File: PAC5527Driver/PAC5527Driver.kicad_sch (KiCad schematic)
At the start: 80 parts, among them J1 Conn_01x08, J2 Conn_01x04, J3 Conn_01x04, J4 Conn_01x02, U1 USBLC6-2SC6, U2 SN65HVD230, U3 MA730, U4 PAC5527, U5 HT7550-1-SOT89

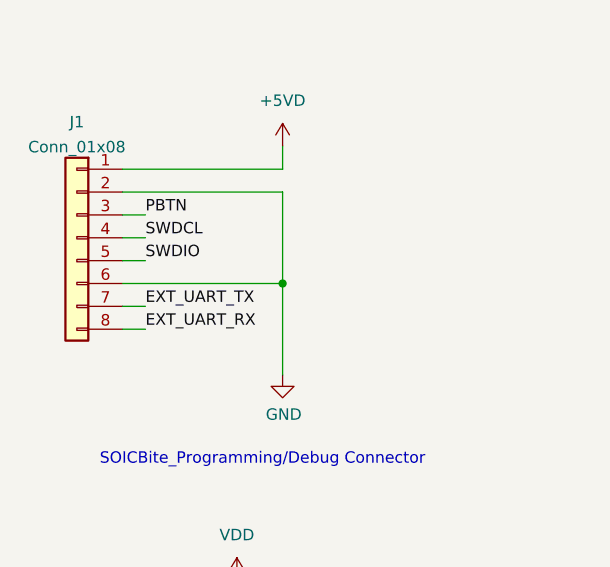
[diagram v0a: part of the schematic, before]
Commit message: MCU fanout, power stage roughed in, setup is now 6L
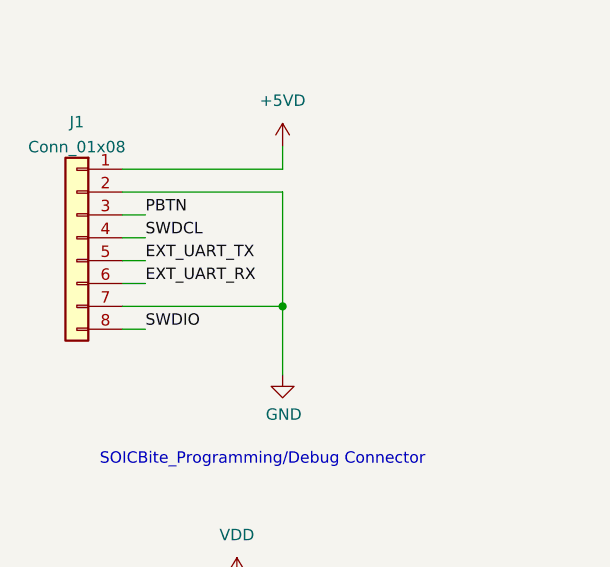
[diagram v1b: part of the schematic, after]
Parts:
- L1: footprint Inductor_SMD:L_Bourns-SRN4018 -> Inductor_SMD:L_Changjiang_FNR3010S
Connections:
- net EXT_UART_RX: now also J1.6 (Pin_6); no longer J1.8 (Pin_8)
- net EXT_UART_TX: now also J1.5 (Pin_5); no longer J1.7 (Pin_7)
- net GND: now also J1.7 (Pin_7); no longer J1.6 (Pin_6)
- net SWDIO: now also J1.8 (Pin_8); no longer J1.5 (Pin_5)
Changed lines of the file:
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@@
   (junction (at 129.54 162.56) (diameter 0) (color 0 0 0 0)
   )
-  (junction (at 55.88 55.88) (diameter 0) (color 0 0 0 0)
-  )
   (junction (at 163.83 247.65) (diameter 0) (color 0 0 0 0)
   )
@@
   )
   (junction (at 193.04 38.1) (diameter 0) (color 0 0 0 0)
+  )
+  (junction (at 55.88 58.42) (diameter 0) (color 0 0 0 0)
   )
   (junction (at 368.3 132.08) (diameter 0) (color 0 0 0 0)
@@
     (stroke (width 0) (type default))
   )
+  (wire (pts (xy 38.1 55.88) (xy 40.64 55.88))
+    (stroke (width 0) (type default))
+  )
   (wire (pts (xy 133.35 262.89) (xy 133.35 257.81))
     (stroke (width 0) (type default))
@@
     (stroke (width 0) (type default))
   )
+  (wire (pts (xy 38.1 58.42) (xy 55.88 58.42))
+    (stroke (width 0) (type default))
+  )
   (wire (pts (xy 227.33 147.32) (xy 242.57 147.32))
     (stroke (width 0) (type default))
@@
     (stroke (width 0) (type default))
   )
+  (wire (pts (xy 55.88 58.42) (xy 55.88 66.04))
+    (stroke (width 0) (type default))
+  )
   (wire (pts (xy 248.92 262.89) (xy 260.35 262.89))
     (stroke (width 0) (type default))
@@
     (stroke (width 0) (type default))
   )
-  (wire (pts (xy 55.88 55.88) (xy 55.88 66.04))
+  (wire (pts (xy 55.88 45.72) (xy 55.88 58.42))
     (stroke (width 0) (type default))
   )
@@
     (stroke (width 0) (type default))
   )
-  (wire (pts (xy 38.1 58.42) (xy 40.64 58.42))
-    (stroke (width 0) (type default))
-  )
   (wire (pts (xy 368.3 60.96) (xy 368.3 66.04))
     (stroke (width 0) (type default))
@@
     (stroke (width 0) (type default))
   )
-  (wire (pts (xy 55.88 45.72) (xy 55.88 55.88))
-    (stroke (width 0) (type default))
-  )
   (wire (pts (xy 342.9 132.08) (xy 342.9 134.62))
     (stroke (width 0) (type default))
@@
   )
   (wire (pts (xy 205.74 144.78) (xy 205.74 147.32))
-    (stroke (width 0) (type default))
-  )
-  (wire (pts (xy 38.1 55.88) (xy 55.88 55.88))
     (stroke (width 0) (type default))
   )
@@
     (effects (font (size 1.27 1.27)) (justify left bottom))
   )
-  (label "EXT_UART_RX" (at 40.64 60.96 0) (fields_autoplaced)
-    (effects (font (size 1.27 1.27)) (justify left bottom))
-  )
   (label "ENC_MISO" (at 292.1 78.74 0) (fields_autoplaced)
     (effects (font (size 1.27 1.27)) (justify left bottom))
   )
   (label "LED_IN" (at 292.1 66.04 0) (fields_autoplaced)
+    (effects (font (size 1.27 1.27)) (justify left bottom))
+  )
+  (label "EXT_UART_RX" (at 40.64 55.88 0) (fields_autoplaced)
     (effects (font (size 1.27 1.27)) (justify left bottom))
   )
@@
     (effects (font (size 1.27 1.27)) (justify left bottom))
   )
-  (label "EXT_UART_TX" (at 40.64 58.42 0) (fields_autoplaced)
-    (effects (font (size 1.27 1.27)) (justify left bottom))
-  )
   (label "US" (at 347.98 50.8 0) (fields_autoplaced)
     (effects (font (size 1.27 1.27)) (justify left bottom))
   )
+  (label "SWDIO" (at 40.64 60.96 0) (fields_autoplaced)
+    (effects (font (size 1.27 1.27)) (justify left bottom))
+  )
   (label "CAN_L" (at 172.72 149.86 0) (fields_autoplaced)
     (effects (font (size 1.27 1.27)) (justify left bottom))
@@
     (effects (font (size 1.27 1.27)) (justify left bottom))
   )
+  (label "EXT_UART_TX" (at 40.64 53.34 0) (fields_autoplaced)
+    (effects (font (size 1.27 1.27)) (justify left bottom))
+  )
   (label "UART_RX" (at 292.1 43.18 0) (fields_autoplaced)
     (effects (font (size 1.27 1.27)) (justify left bottom))
@@
   )
   (label "VH" (at 294.64 124.46 0) (fields_autoplaced)
-    (effects (font (size 1.27 1.27)) (justify left bottom))
-  )
-  (label "SWDIO" (at 40.64 53.34 0) (fields_autoplaced)
     (effects (font (size 1.27 1.27)) (justify left bottom))
   )
@@
       (effects (font (size 1.27 1.27)))
     )
-    (property "Footprint" "Inductor_SMD:L_Bourns-SRN4018" (at 113.03 38.1 0)
+    (property "Footprint" "Inductor_SMD:L_Changjiang_FNR3010S" (at 113.03 38.1 0)
       (effects (font (size 1.27 1.27)) hide)
     )

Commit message: output via stitching
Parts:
- D3: footprint Diode_SMD:D_SMA -> Diode_SMD:D_SOD-123
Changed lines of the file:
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@@
       (effects (font (size 1.27 1.27)) (justify left))
     )
-    (property "Footprint" "Diode_SMD:D_SMA" (at 60.96 209.55 0)
+    (property "Footprint" "Diode_SMD:D_SOD-123" (at 60.96 209.55 0)
       (effects (font (size 1.27 1.27)) hide)
     )

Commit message: initial layout pass
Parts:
- removed C15, C17, C28: 10uF, Capacitor_SMD:C_1210_3225Metric, symbol Device:C
- removed R20, R21, R22: 0.1, Resistor_SMD:R_1206_3216Metric, symbol Device:R
- added R20, R21, R22: 0.1, PAC5527Driver:RShunt_1206_3216Metric, symbol Device:R_Shunt
- C7: footprint Capacitor_SMD:C_0603_1608Metric -> Capacitor_SMD:C_0402_1005Metric
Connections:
- net GND: now also R20.4, R21.4, R22.4; no longer RN1.1 (R1.1), RN1.3 (R3.1), RN1.5 (R5.1)
- net at Q1.SL: now also R20.1; no longer RN1.2 (R2.1)
- net at Q2.SL: now also R21.1; no longer RN1.4 (R4.1)
- net at Q3.SL: now also R22.1; no longer RN1.6 (R6.1)
- new net: R20.2, RN1.2 (R2.1)
- new net: R21.2, RN1.4 (R4.1)
- new net: R22.3, RN1.5 (R5.1)
- new net: R22.2, RN1.6 (R6.1)
- new net: R20.3, RN1.1 (R1.1)
- new net: R21.3, RN1.3 (R3.1)
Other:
- moved on the sheet: C19, C22, C23, C24, C27, C29, C30, C31, C32, C33, C34, C39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

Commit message: redone layout
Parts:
- removed C22, C39, C40: 10uF, Capacitor_SMD:C_1210_3225Metric, symbol Device:C
- removed D6: NUP2105L, Package_TO_SOT_SMD:SOT-23, symbol Power_Protection:NUP2105L
- removed J2, J3: Conn_01x04, Connector_JST:JST_GH_SM04B-GHS-TB_1x04-1MP_P1.25mm_Horizontal, symbol Connector_Generic:Conn_01x04
- removed R10, R8: 10k, Resistor_SMD:R_0402_1005Metric, symbol Device:R
- removed R7: 100, Resistor_SMD:R_0402_1005Metric, symbol Device:R
- removed U2: SN65HVD230, Package_SO:SOIC-8_3.9x4.9mm_P1.27mm, symbol Interface_CAN_LIN:SN65HVD230
- removed U5: HT7550-1-SOT89, Package_TO_SOT_SMD:SOT-89-3, symbol Regulator_Linear:HT75xx-1-SOT89
- added C15, C17, C21, C26, C28, C35, C36, C37, C38: 10uF, Capacitor_SMD:C_1210_3225Metric, symbol Device:C
- added D5: NUP2105L, Package_TO_SOT_SMD:SOT-23, symbol Power_Protection:NUP2105L
- added J2, J3: Conn_01x04_MountingPin, Connector_JST:JST_GH_SM04B-GHS-TB_1x04-1MP_P1.25mm_Horizontal, symbol Connector_Generic_MountingPin:Conn_01x04_MountingPin
- added J5: Conn_01x06_MountingPin, Connector_JST:JST_GH_BM06B-GHS-TBT_1x06-1MP_P1.25mm_Vertical, symbol Connector_Generic_MountingPin:Conn_01x06_MountingPin
- added J6: Conn_01x03, Connector_PinHeader_2.54mm:PinHeader_1x03_P2.54mm_Vertical, symbol Connector_Generic:Conn_01x03
- added J8: Conn_01x03_MountingPin, Connector_JST:JST_GH_BM03B-GHS-TBT_1x03-1MP_P1.25mm_Vertical, symbol Connector_Generic_MountingPin:Conn_01x03_MountingPin
- added R2: 10k, Resistor_SMD:R_0402_1005Metric, symbol Device:R
- added R4: 100, Resistor_SMD:R_0402_1005Metric, symbol Device:R
- added U2: TCAN330G, Package_TO_SOT_SMD:SOT-23-8, symbol Interface_CAN_LIN:TCAN330G
- added U6: HT7533-1-SOT89, Package_TO_SOT_SMD:SOT-89-3, symbol Regulator_Linear:HT75xx-1-SOT89
- H1, H2: footprint PAC5527Driver:MountingHole_SLOT_1.6_M1.5_DIN965_Pad_TopBottom -> MountingHole:MountingHole_2.2mm_M2_DIN965_Pad_TopBottom
- H3, H4, H5: footprint PAC5527Driver:MountingHole_SLOT_2.2mm_M2_DIN965_Pad_TopBottom -> MountingHole:MountingHole_2.2mm_M2_DIN965_Pad_TopOnly
- R9: value 100 -> 10k
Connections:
- net +12V: now also U6.2 (VIN)
- net CAN_H: now also D5.1 (K), J2.2 (Pin_2), J3.2 (Pin_2), R2.1, U2.7 (CANH)
- net CAN_L: now also D5.2 (K), J2.3 (Pin_3), J3.3 (Pin_3), R2.2, U2.6 (CANL)
- net CAN_SLP: now also R4.1
- net ENC_MISO: now also J5.5 (Pin_5)
- net ENC_MOSI: now also J5.4 (Pin_4)
- net ENC_SCLK: now also J5.2 (Pin_2)
- net EXT_UART_RX: now also J6.2 (Pin_2)
- net EXT_UART_TX: now also J6.3 (Pin_3)
- net GND: now also C4.2, C15.2, C17.2, C21.2, C26.2, C28.2, C35.2, C36.2, C37.2, C38.2, D5.3 (A), J2.1 (Pin_1), J2.MP (MountPin), J3.1 (Pin_1), J3.MP (MountPin), J5.6 (Pin_6), J5.MP (MountPin), J6.1 (Pin_1), J8.3 (Pin_3), J8.MP (MountPin), U2.2 (GND), U6.1 (GND); no longer C4.1
- net MB_ID_0: now also J8.2 (Pin_2)
- net MB_ID_1: now also J8.1 (Pin_1)
- net VDC: now also C15.1, C17.1, C21.1, C26.1, C28.1, C35.1, C36.1, C37.1, C38.1
- net VDD: now also J5.1 (Pin_1), U2.3 (VCC), U6.3 (VOUT)
- net ENC_CS1: now reaches U4.35 (PD5)
- net ENC_CS1: now also J5.3 (Pin_3)
- net at R5.1: now also U2.1 (TXD)
- net at R6.2: now also U2.4 (RXD)
- new net: C4.1, R4.2, U2.8 (S)
- no-connect marks 17 -> 18
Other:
- moved on the sheet: C14, C19, C20, C25, C5, C8, D1, D2, D3, D4, H1, H2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

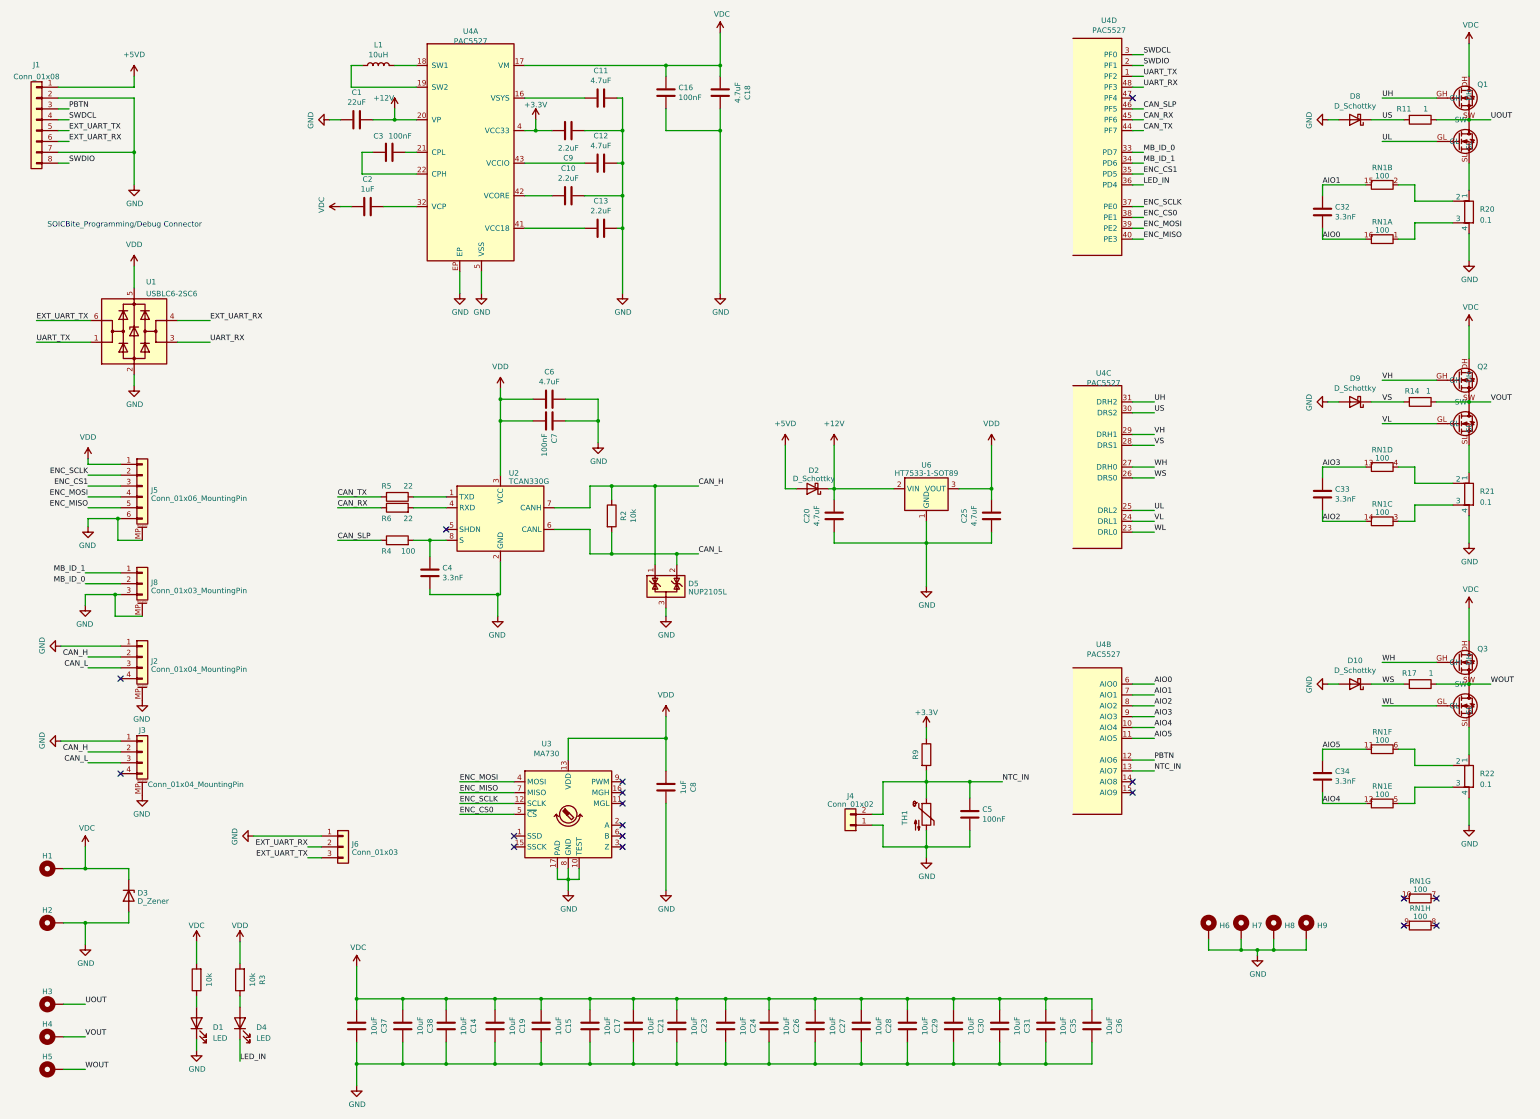
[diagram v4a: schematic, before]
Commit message: spaced out mounting points by 0.5mm
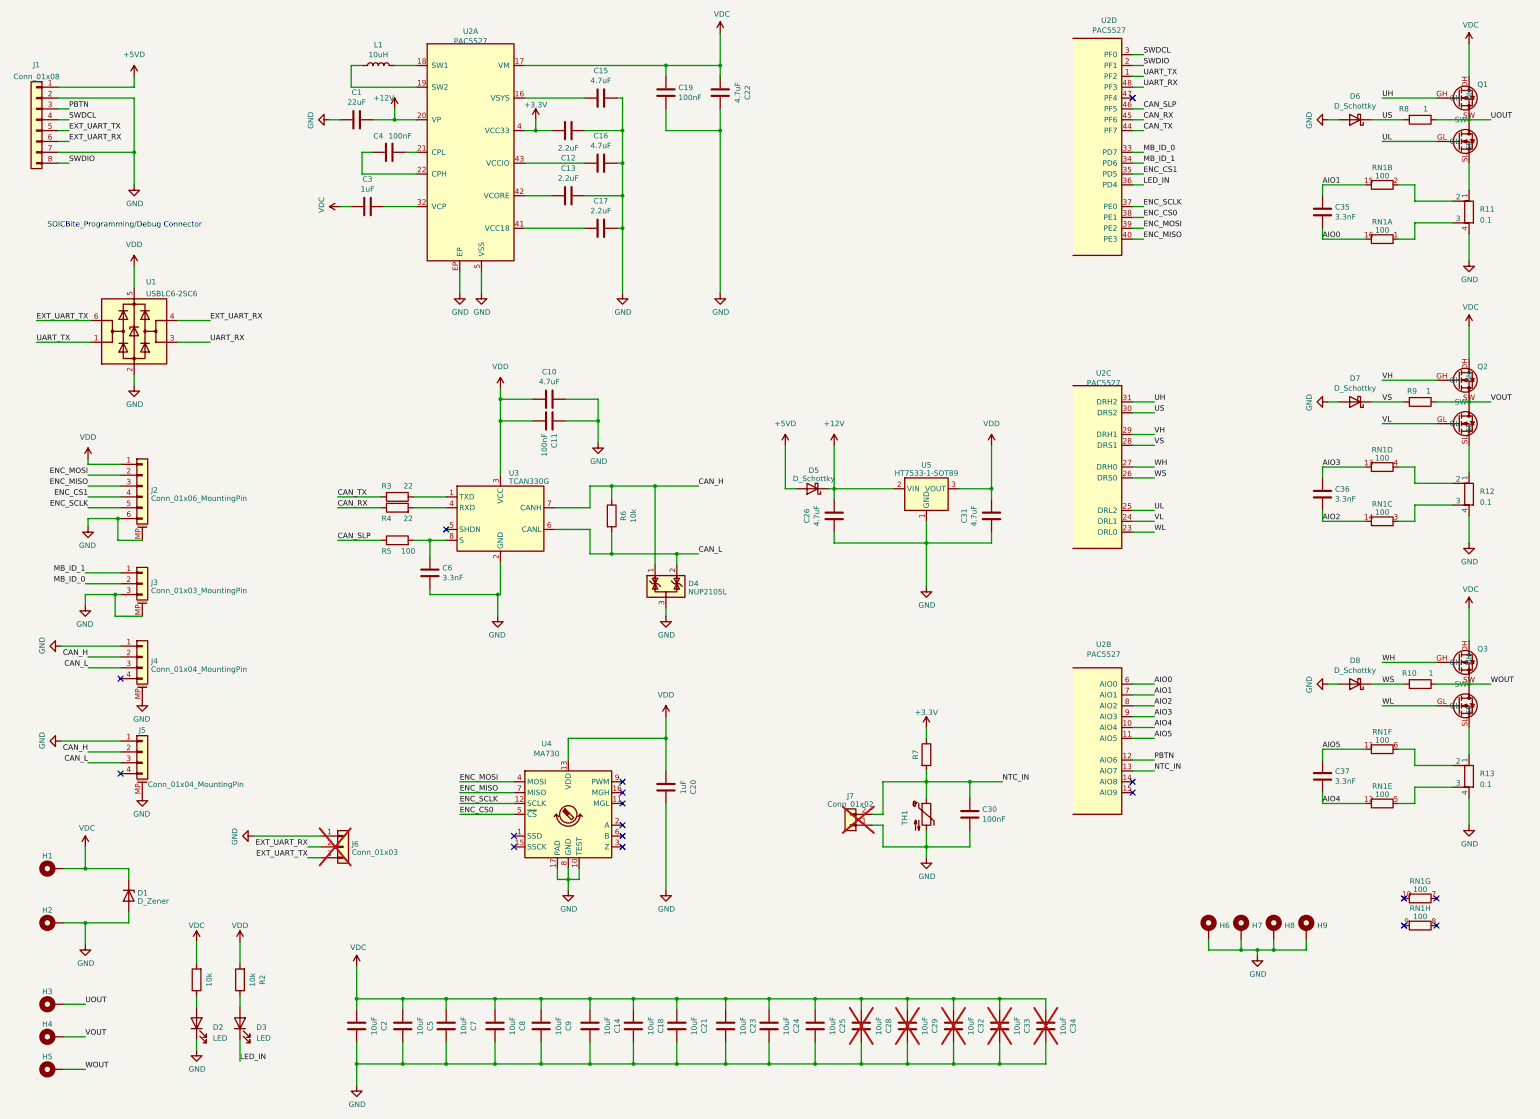
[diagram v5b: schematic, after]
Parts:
- removed C28: 10uF, Capacitor_SMD:C_1210_3225Metric, symbol Device:C
- C28: renamed from C29; now not fitted
- C29: renamed from C30; now not fitted
- C32: renamed from C31; now not fitted
- C33: renamed from C35; now not fitted
- C34: renamed from C36; now not fitted
- H6, H7, H8, H9: footprint MountingHole:MountingHole_2.2mm_M2_ISO7380_Pad_TopBottom -> MountingHole:MountingHole_2.7mm_M2.5_DIN965_Pad_TopBottom
- J6: now not fitted
- J7: renamed from J4; now not fitted
- renumbered C6 to C10, C7 to C11, C9 to C12, C10 to C13, C17 to C14, C11 to C15, C12 to C16, C13 to C17, C21 to C18, C16 to C19, C37 to C2, C8 to C20, C23 to C21, C18 to C22, C24 to C23, C26 to C24, C27 to C25, C20 to C26, C2 to C3, C5 to C30, C25 to C31, C32 to C35, C33 to C36, C34 to C37, C3 to C4, C38 to C5, C4 to C6, C14 to C7, C19 to C8, C15 to C9, D3 to D1, D1 to D2, D4 to D3, D5 to D4, D2 to D5, D8 to D6, D9 to D7, D10 to D8, J5 to J2, J8 to J3, J2 to J4, J3 to J5, R17 to R10, R20 to R11, R21 to R12, R22 to R13, R3 to R2, R5 to R3, R6 to R4, R4 to R5, R2 to R6, R9 to R7, R11 to R8, R14 to R9, U4 to U2, U2 to U3, U3 to U4, U6 to U5
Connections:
- net ENC_CS1: now also J2.4 (Pin_4); no longer J2.3 (Pin_3)
- net ENC_MISO: now also J2.3 (Pin_3); no longer J2.5 (Pin_5)
- net ENC_MOSI: now also J2.2 (Pin_2); no longer J2.4 (Pin_4)
- net ENC_SCLK: now also J2.5 (Pin_5); no longer J2.2 (Pin_2)

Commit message: initial layout
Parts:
- removed C21, C23, C24, C28, C29, C32, C33, C34: 10uF, Capacitor_SMD:C_1210_3225Metric, symbol Device:C
- removed C6: 3.3nF, Capacitor_SMD:C_0402_1005Metric, symbol Device:C
- removed J2: Conn_01x06_MountingPin, Connector_JST:JST_GH_BM06B-GHS-TBT_1x06-1MP_P1.25mm_Vertical, symbol Connector_Generic_MountingPin:Conn_01x06_MountingPin
- removed Q1, Q2, Q3: ~, PAC5527Driver:PG-TDSON-8, symbol PAC5527_MD:IAUC60N04S6L045H
- removed R11, R12, R13: 0.1, PAC5527Driver:RShunt_1206_3216Metric, symbol Device:R_Shunt
- removed U3: TCAN330G, Package_TO_SOT_SMD:SOT-23-8, symbol Interface_CAN_LIN:TCAN330G
- added C12, C14, C15, C17: 10uF, Capacitor_SMD:C_1210_3225Metric, symbol Device:C
- added C3: 100nF, Capacitor_SMD:C_0402_1005Metric, symbol Device:C
- added J2: Conn_01x04_MountingPin, Connector_JST:JST_GH_BM04B-GHS-TBT_1x04-1MP_P1.25mm_Vertical, symbol Connector_Generic_MountingPin:Conn_01x04_MountingPin
- added J3: Conn_01x08_MountingPin, Connector_JST:JST_GH_BM08B-GHS-TBT_1x08-1MP_P1.25mm_Vertical, symbol Connector_Generic_MountingPin:Conn_01x08_MountingPin
- added NT1, NT2, NT3, NT4, NT5, NT6: NetTie_2, NetTie:NetTie-2_SMD_Pad0.5mm, symbol Device:NetTie_2
- added Q1, Q2, Q3, Q4, Q5, Q6: Si7336ADP, Package_SO:PowerPAK_SO-8_Single, symbol Transistor_FET:Si7336ADP
- added R13, R14, R15: R, Resistor_SMD:R_2512_6332Metric, symbol Device:R
- added R5: 100, Resistor_SMD:R_0402_1005Metric, symbol Device:R
- added R7: 10k, Resistor_SMD:R_0402_1005Metric, symbol Device:R
- added U2: SN65HVD233, Package_SO:SOIC-8_3.9x4.9mm_P1.27mm, symbol Interface_CAN_LIN:SN65HVD233
- H6, H7, H8, H9: footprint MountingHole:MountingHole_2.7mm_M2.5_DIN965_Pad_TopBottom -> MountingHole:MountingHole_2.7mm_M2.5_Pad_TopBottom
- R6: renamed from R5; value 100 -> 10k
- renumbered C2 to C1, C1 to C10, C3 to C11, C4 to C13, C20 to C16, C26 to C19, C5 to C2, C12 to C20, C13 to C21, C15 to C22, C16 to C23, C17 to C24, C19 to C26, C22 to C27, C31 to C28, C30 to C29, C37 to C30, C36 to C31, C35 to C32, C7 to C4, C8 to C5, C9 to C6, C10 to C7, C11 to C8, C14 to C9, D8 to D6, D6 to D8, J3 to J4, J4 to J5, J5 to J6, J6 to J7, J7 to J8, R9 to R11, R8 to R12, R6 to R8, R7 to R9, U4 to U3, U2 to U4
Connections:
- net CAN_H: now also U2.7 (CANH)
- net CAN_L: now also U2.6 (CANL)
- net ENC_CS1: now also J3.7 (Pin_7)
- net ENC_MISO: now also J3.6 (Pin_6)
- net ENC_MOSI: now also J3.5 (Pin_5)
- net ENC_SCLK: now also J3.8 (Pin_8)
- net EXT_UART_RX: now also J3.4 (Pin_4)
- net EXT_UART_TX: now also J3.3 (Pin_3)
- net GND: now also R6.1, C12.2, C14.2, C15.2, C17.2, C3.1, J2.4 (Pin_4), J2.MP (MountPin), J3.1 (Pin_1), J3.MP (MountPin), NT2.2, NT4.2, NT6.2, R13.2, R14.2, R15.2, R7.1, U2.2 (GND)
- net SWDCL: now also J2.2 (Pin_2)
- net SWDIO: now also J2.3 (Pin_3)
- net UH: now also Q5.4 (G)
- net UL: now also Q6.4 (G)
- net UOUT: now also Q5.1 (S), Q5.2 (S), Q5.3 (S), Q6.5 (D)
- net VDC: now also C12.1, C14.1, C15.1, C17.1, Q1.5 (D), Q3.5 (D), Q5.5 (D)
- net VDD: now also J2.1 (Pin_1), J3.2 (Pin_2), U2.3 (VCC)
- net VH: now also Q3.4 (G)
- net VL: now also Q4.4 (G)
- net VOUT: now also Q3.1 (S), Q3.2 (S), Q3.3 (S), Q4.5 (D)
- net WH: now also Q1.4 (G)
- net WL: now also Q2.4 (G)
- net WOUT: now also Q1.1 (S), Q1.2 (S), Q1.3 (S), Q2.5 (D)
- net at R6.2: now also C3.2, R5.2, U2.8 (Rs)
- net at RN1.2 (R2.1): now also NT5.1
- net at RN1.4 (R4.1): now also NT3.1
- net at RN1.5 (R5.1): now also NT2.1
- net at RN1.6 (R6.1): now also NT1.1
- net at RN1.1 (R1.1): now also NT6.1
- net at R4.2: now also U2.4 (R)
- net at RN1.3 (R3.1): now also NT4.1
- net at R3.1: now also U2.1 (D)
- net CAN_SLP renamed CAN_STDBY
- net CAN_STDBY: now also R5.1; no longer R6.1
- new net: NT3.2, Q4.1 (S), Q4.2 (S), Q4.3 (S), R14.1
- new net: NT1.2, Q2.1 (S), Q2.2 (S), Q2.3 (S), R13.1
- new net: R7.2, U2.5 (LBK)
- new net: NT5.2, Q6.1 (S), Q6.2 (S), Q6.3 (S), R15.1
- no-connect marks 18 -> 17
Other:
- moved on the sheet: C10, C11, C13, C16, C2, C20, C21, C22, C23, C24, C26, C27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

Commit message: layout complete
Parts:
- removed D1: D_Zener, Diode_SMD:D_SOD-123, symbol Device:D_Zener
- removed J7: Conn_01x03, Connector_PinHeader_2.54mm:PinHeader_1x03_P2.54mm_Vertical, symbol Connector_Generic:Conn_01x03
- added J6, J8: Conn_01x04_MountingPin, Connector_JST:JST_GH_BM04B-GHS-TBT_1x04-1MP_P1.25mm_Vertical, symbol Connector_Generic_MountingPin:Conn_01x04_MountingPin
- renumbered C26 to C1, C11 to C10, C24 to C11, C7 to C12, C8 to C13, C31 to C14, C19 to C15, C28 to C16, C3 to C17, C32 to C18, C16 to C19, C27 to C2, C29 to C20, C1 to C21, C2 to C22, C4 to C23, C5 to C24, C6 to C25, C9 to C26, C12 to C27, C14 to C28, C15 to C29, C22 to C3, C17 to C30, C18 to C31, C25 to C32, C10 to C4, C20 to C5, C13 to C6, C23 to C7, C21 to C8, C30 to C9, D6 to D1, D7 to D2, D5 to D3, D8 to D5, D2 to D6, D3 to D7, H6 to H3, H7 to H4, H8 to H5, H9 to H6, H3 to H7, H4 to H8, H5 to H9, J6 to J7, J8 to J9, R10 to R1, R7 to R10, R12 to R11, R15 to R12, R9 to R13, R1 to R14, R2 to R15, R13 to R2, R11 to R3, R14 to R4, R3 to R5, R4 to R6, R8 to R7, R5 to R8, R6 to R9, U4 to U2, U5 to U3, U2 to U4, U3 to U5
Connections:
- net CAN_H: now also J6.2 (Pin_2), J8.2 (Pin_2)
- net CAN_L: now also J6.3 (Pin_3), J8.3 (Pin_3)
- net GND: now also J6.1 (Pin_1), J6.MP (MountPin), J8.1 (Pin_1), J8.MP (MountPin)
- no-connect marks 17 -> 19
